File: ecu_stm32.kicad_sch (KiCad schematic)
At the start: 11 parts, among them J3 ARM Cortex Debug, U8 AZ1117-3.3

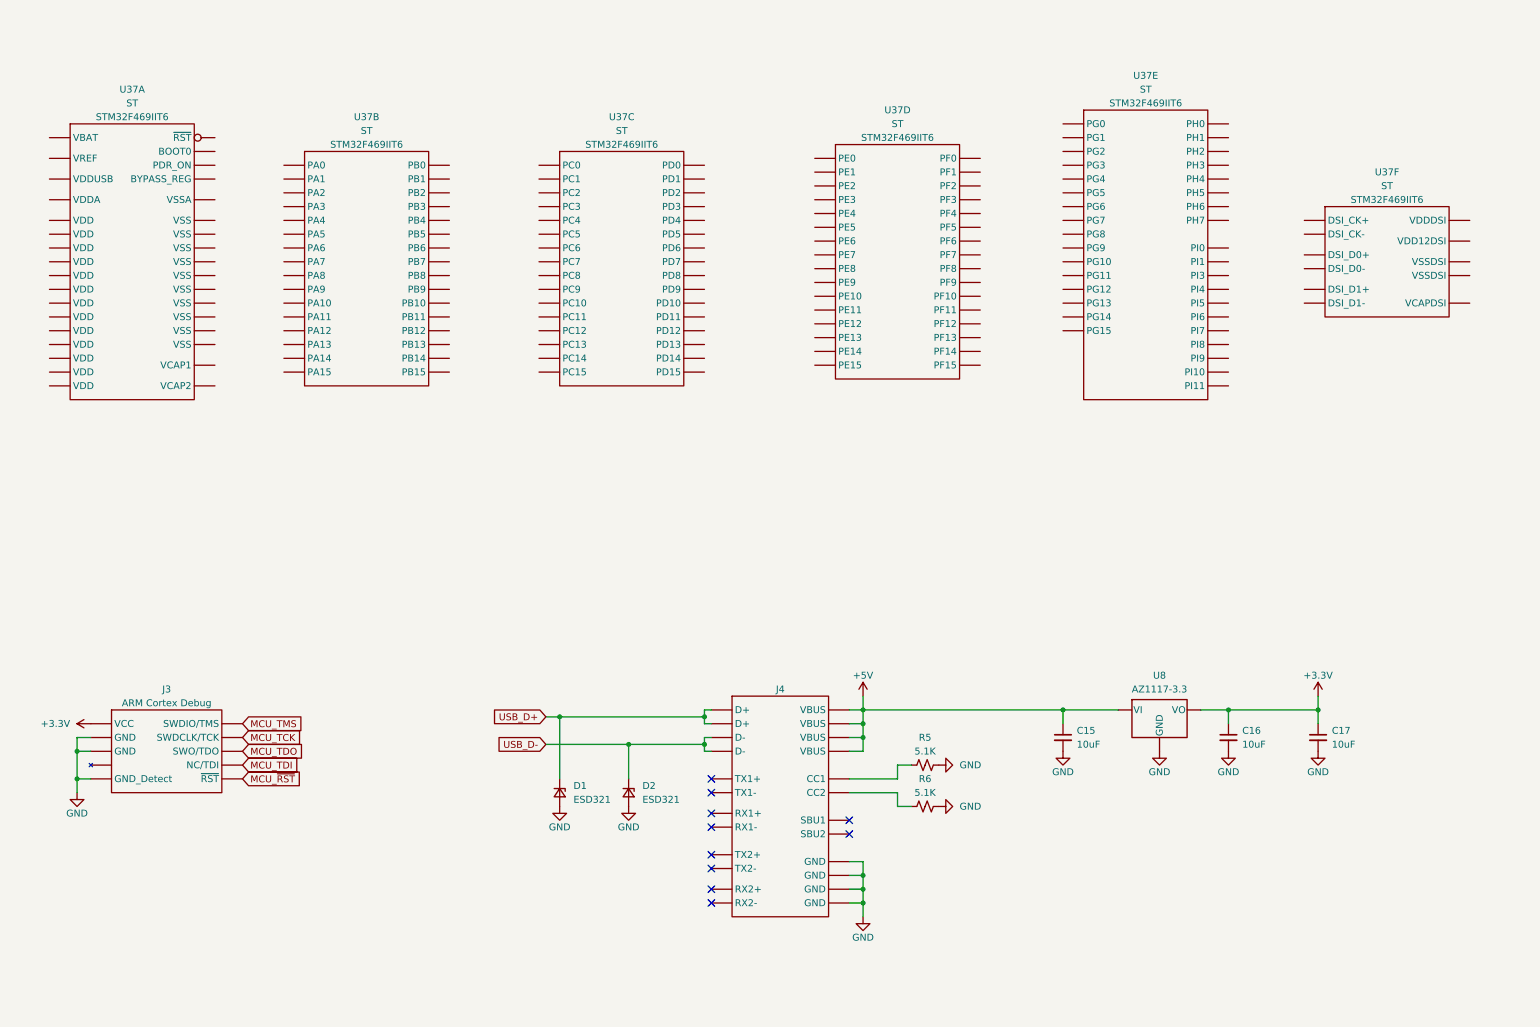
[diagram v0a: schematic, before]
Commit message: changed usb-c, re-named and added some pins
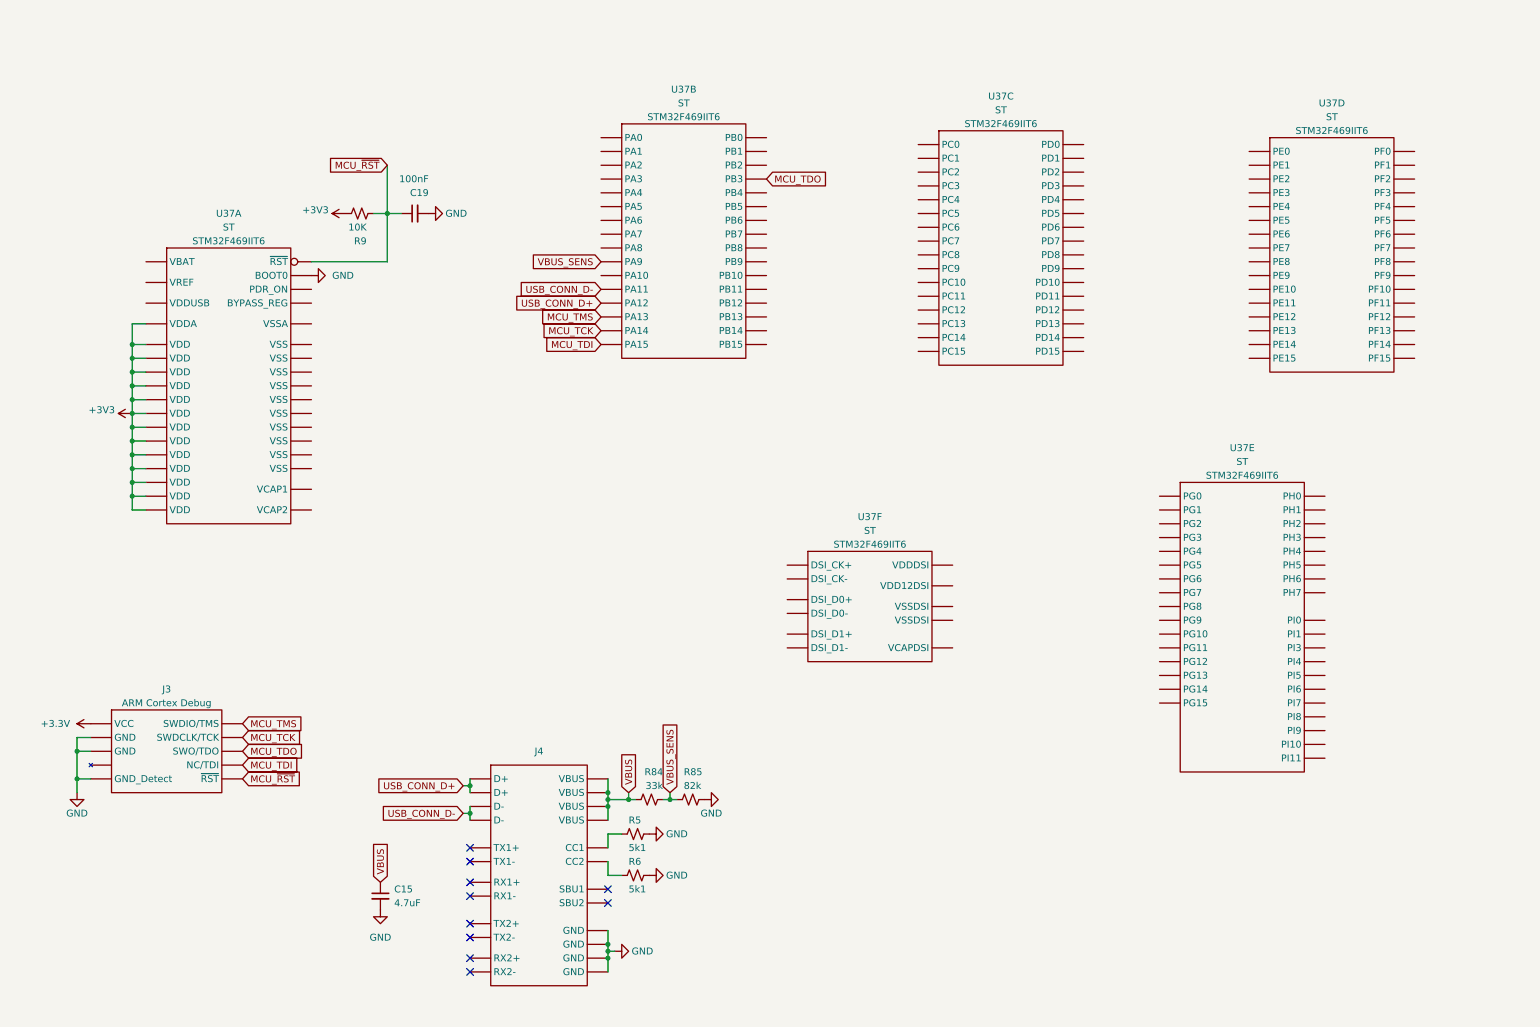
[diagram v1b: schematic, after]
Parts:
- removed C16, C17: 10uF, Capacitor_SMD:C_0603_1608Metric, symbol Device:C_Small
- removed D1, D2: ESD321, Diode_SMD:D_0402_1005Metric, symbol Device:D_Zener_Small
- removed U8: AZ1117-3.3, Package_TO_SOT_SMD:SOT-223-3_TabPin2, symbol Regulator_Linear:AZ1117-3.3
- added C19: 100nF, Capacitor_SMD:C_0603_1608Metric_Pad1.08x0.95mm_HandSolder, symbol Device:C_Small
- added R84: 33k, Resistor_SMD:R_0603_1608Metric, symbol Device:R_Small_US
- added R85: 82k, Resistor_SMD:R_0603_1608Metric, symbol Device:R_Small_US
- added R9: 10K, Resistor_SMD:R_0603_1608Metric_Pad0.98x0.95mm_HandSolder, symbol Device:R_Small_US
- C15: value 10uF -> 4.7uF; Part # Generic 0603 10uF 6.3V X7R MLCC -> Generic 0603 6.3V 4.7uF X7R MLCC
- R5, R6: value 5.1K -> 5k1; Part # Generic 0603 5.1K 1% Resistor -> Generic 0603 5.1k 1% Resistor
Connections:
- net USB_D+ is gone; now on net USB_CONN_D+: J4.A6 (D+), J4.B6 (D+)
- net USB_D- is gone; now on net USB_CONN_D-: J4.A7 (D-), J4.B7 (D-)
- net GND: now also R5.1, R6.1, U37.166 (BOOT0), C19.2, R85.1; no longer R5.2, R6.2
- net MCU_TCK: now also U37.137 (PA14)
- net MCU_TDI: now also U37.138 (PA15)
- net MCU_TDO: now also U37.161 (PB3)
- net MCU_TMS: now also U37.128 (PA13)
- net MCU_~{RST}: now also U37.31 (~{RST}), C19.1, R9.2
- net at J4.B5 (CC2): now also R6.2; no longer R6.1
- net +3V3: now reaches U37.131 (VDD)
- net +3V3: now also U37.136 (VDD), U37.149 (VDD), U37.15 (VDD), U37.159 (VDD), U37.172 (VDD), U37.23 (VDD), U37.36 (VDD), U37.39 (VDDA), U37.49 (VDD), U37.62 (VDD), U37.72 (VDD), U37.82 (VDD), U37.96 (VDD), R9.1
- net at J4.A5 (CC1): now also R5.2; no longer R5.1
- net VBUS_SENS: now reaches U37.124 (PA9)
- net VBUS_SENS: now also R84.2, R85.2
- net USB_CONN_D-: now reaches U37.126 (PA11)
- net USB_CONN_D+: now reaches U37.127 (PA12)
- net +5V renamed VBUS
- net VBUS: now also R84.1
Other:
- moved on the sheet: U37A, U37B, U37C, U37D, U37E, U37F

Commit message: added pin assignments to components on existing schematic
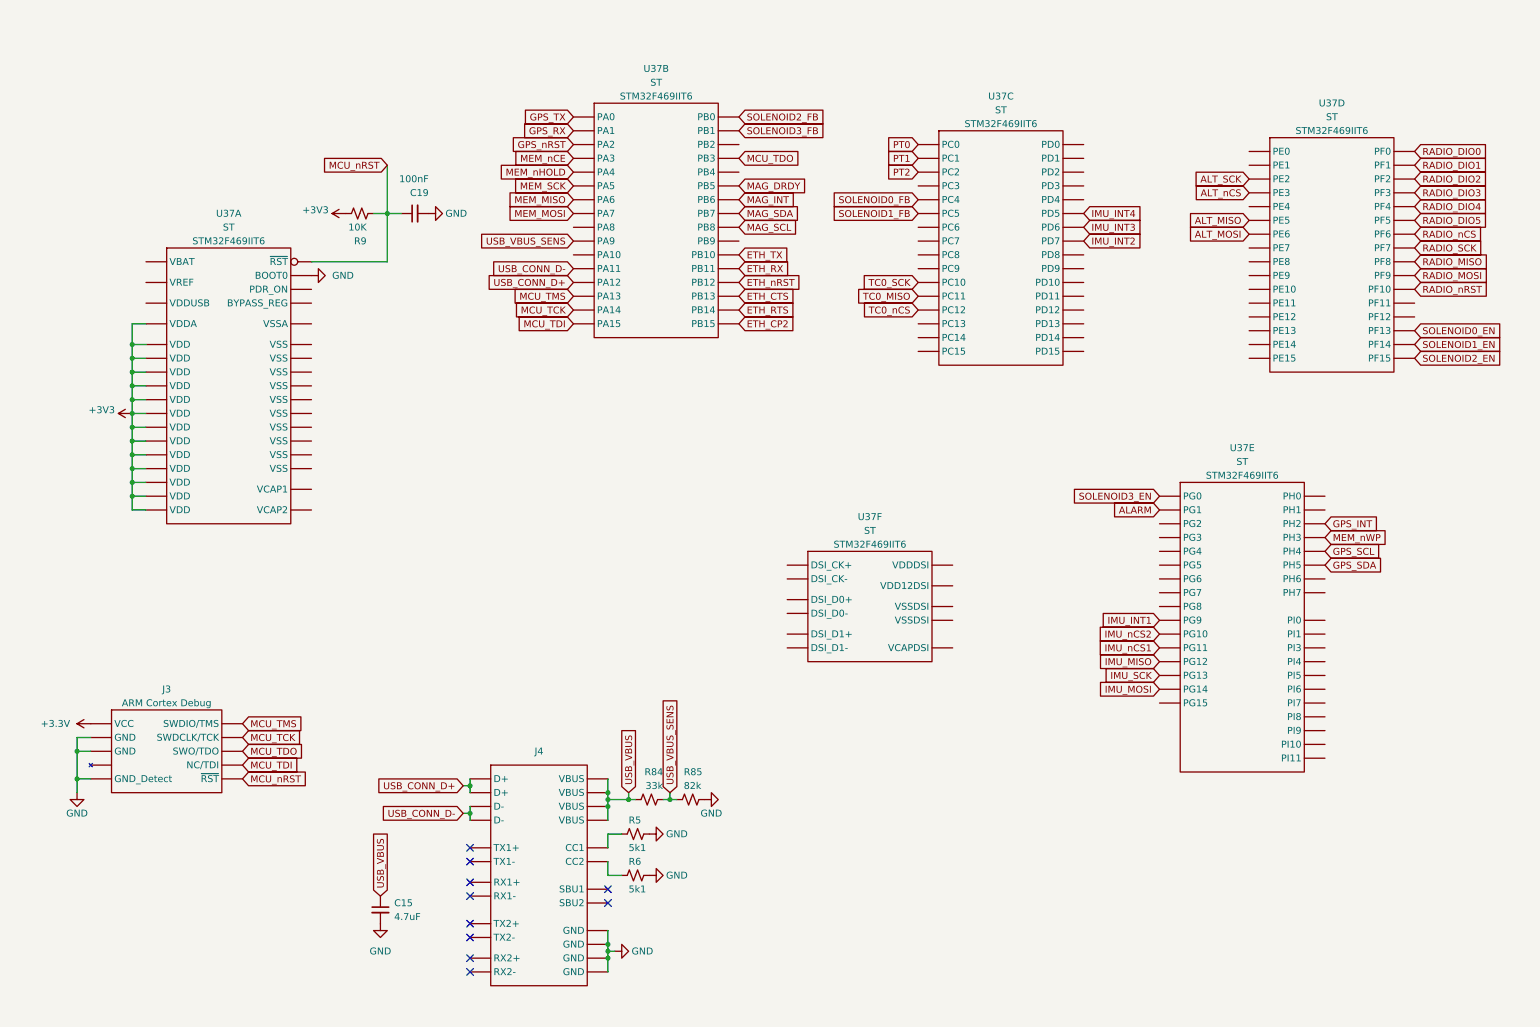
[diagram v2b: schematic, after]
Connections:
- net TC0_SCK: now reaches U37.139 (PC10)
- net TC0_MISO: now reaches U37.140 (PC11)
- net TC0_nCS: now reaches U37.141 (PC12)
- net IMU_INT4: now reaches U37.147 (PD5)
- net IMU_INT3: now reaches U37.150 (PD6)
- net IMU_INT2: now reaches U37.151 (PD7)
- net PT0: now reaches U37.32 (PC0)
- net PT1: now reaches U37.33 (PC1)
- net PT2: now reaches U37.34 (PC2)
- net SOLENOID0_FB: now reaches U37.54 (PC4)
- net SOLENOID1_FB: now reaches U37.55 (PC5)
- net IMU_INT1: now reaches U37.152 (PG9)
- net IMU_nCS2: now reaches U37.153 (PG10)
- net IMU_nCS1: now reaches U37.154 (PG11)
- net IMU_MISO: now reaches U37.155 (PG12)
- net IMU_SCK: now reaches U37.156 (PG13)
- net IMU_MOSI: now reaches U37.157 (PG14)
- net GPS_INT: now reaches U37.43 (PH2)
- net MEM_nWP: now reaches U37.44 (PH3)
- net GPS_SCL: now reaches U37.45 (PH4)
- net GPS_SDA: now reaches U37.46 (PH5)
- net SOLENOID3_EN: now reaches U37.66 (PG0)
- net ALARM: now reaches U37.67 (PG1)
- net ALT_SCK: now reaches U37.1 (PE2)
- net RADIO_DIO0: now reaches U37.16 (PF0)
- net RADIO_DIO1: now reaches U37.17 (PF1)
- net RADIO_DIO2: now reaches U37.18 (PF2)
- net RADIO_DIO3: now reaches U37.19 (PF3)
- net ALT_nCS: now reaches U37.2 (PE3)
- net RADIO_DIO4: now reaches U37.20 (PF4)
- net RADIO_DIO5: now reaches U37.21 (PF5)
- net RADIO_nCS: now reaches U37.24 (PF6)
- net RADIO_SCK: now reaches U37.25 (PF7)
- net RADIO_MISO: now reaches U37.26 (PF8)
- net RADIO_MOSI: now reaches U37.27 (PF9)
- net RADIO_nRST: now reaches U37.28 (PF10)
- net ALT_MISO: now reaches U37.4 (PE5)
- net ALT_MOSI: now reaches U37.5 (PE6)
- net SOLENOID0_EN: now reaches U37.63 (PF13)
- net SOLENOID1_EN: now reaches U37.64 (PF14)
- net SOLENOID2_EN: now reaches U37.65 (PF15)
- net MAG_DRDY: now reaches U37.163 (PB5)
- net MAG_INT: now reaches U37.164 (PB6)
- net MAG_SDA: now reaches U37.165 (PB7)
- net MAG_SCL: now reaches U37.167 (PB8)
- net GPS_TX: now reaches U37.40 (PA0)
- net GPS_RX: now reaches U37.41 (PA1)
- net GPS_nRST: now reaches U37.42 (PA2)
- net MEM_nCE: now reaches U37.47 (PA3)
- net MEM_nHOLD: now reaches U37.50 (PA4)
- net MEM_SCK: now reaches U37.51 (PA5)
- net MEM_MISO: now reaches U37.52 (PA6)
- net MEM_MOSI: now reaches U37.53 (PA7)
- net SOLENOID2_FB: now reaches U37.56 (PB0)
- net SOLENOID3_FB: now reaches U37.57 (PB1)
- net ETH_TX: now reaches U37.79 (PB10)
- net ETH_RX: now reaches U37.80 (PB11)
- net ETH_nRST: now reaches U37.85 (PB12)
- net ETH_CTS: now reaches U37.86 (PB13)
- net ETH_RTS: now reaches U37.87 (PB14)
- net ETH_CP2: now reaches U37.88 (PB15)
- net MCU_~{RST} renamed MCU_nRST
- net VBUS renamed USB_VBUS
- net VBUS_SENS renamed USB_VBUS_SENS
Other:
- moved on the sheet: C15, U37B

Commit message: Updated so only STM pins left really
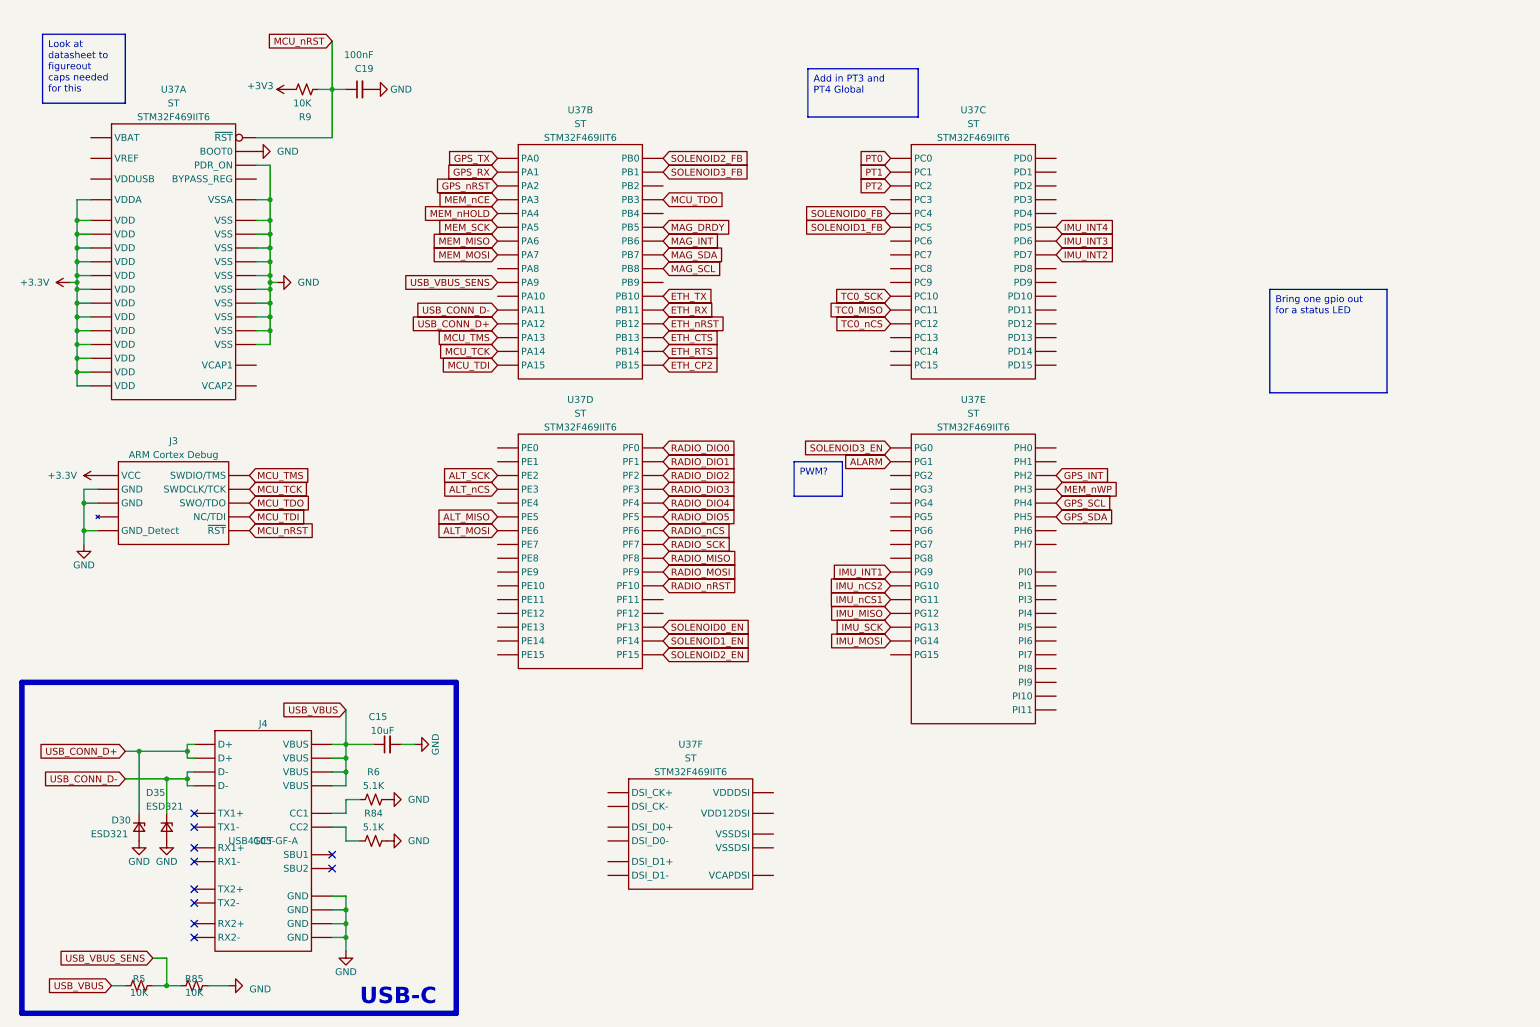
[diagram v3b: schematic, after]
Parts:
- removed J4: ~, Connector_USB:USB_C_Receptacle_GCT_USB4105-xx-A_16P_TopMnt_Horizontal, symbol UCIRP-KiCAD-Lib:USB-C
- added D30, D35: ESD321, Diode_SMD:D_0402_1005Metric, symbol Device:D_Zener_Small
- added J4: ~, Connector_USB:USB_C_Receptacle_GCT_USB4105-xx-A_16P_TopMnt_Horizontal, symbol 0INSP-KICAD-LIB:USB-C
- C15: value 4.7uF -> 10uF; Part # Generic 0603 6.3V 4.7uF X7R MLCC -> Generic 0603 10uF 6.3V X7R MLCC
- R5: value 5k1 -> 10K; footprint Resistor_SMD:R_0603_1608Metric -> Resistor_SMD:R_0603_1608Metric_Pad0.98x0.95mm_HandSolder; Part # Generic 0603 5.1k 1% Resistor -> Generic 0603 10K 1% Resistor
- R6: value 5k1 -> 5.1K; footprint Resistor_SMD:R_0603_1608Metric -> Resistor_SMD:R_0603_1608Metric_Pad0.98x0.95mm_HandSolder; Part # Generic 0603 5.1k 1% Resistor -> Generic 0603 5.1K 1% Resistor
- R84: value 33k -> 5.1K; footprint Resistor_SMD:R_0603_1608Metric -> Resistor_SMD:R_0603_1608Metric_Pad0.98x0.95mm_HandSolder; Part # Generic 0603 33k 1% Resistor -> Generic 0603 5.1K 1% Resistor
- R85: value 82k -> 10K; footprint Resistor_SMD:R_0603_1608Metric -> Resistor_SMD:R_0603_1608Metric_Pad0.98x0.95mm_HandSolder; Part # Generic 0603 82k 1% Resistor -> Generic 0603 10K 1% Resistor
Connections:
- net +3.3V: now also U37.131 (VDD), U37.136 (VDD), U37.149 (VDD), U37.15 (VDD), U37.159 (VDD), U37.172 (VDD), U37.23 (VDD), U37.36 (VDD), U37.39 (VDDA), U37.49 (VDD), U37.62 (VDD), U37.72 (VDD), U37.82 (VDD), U37.96 (VDD)
- net +3V3: no longer U37.131 (VDD), U37.136 (VDD), U37.149 (VDD), U37.15 (VDD), U37.159 (VDD), U37.172 (VDD), U37.23 (VDD), U37.36 (VDD), U37.39 (VDDA), U37.49 (VDD), U37.62 (VDD), U37.72 (VDD), U37.82 (VDD), U37.96 (VDD)
- net GND: now also R6.2, R84.2, R85.2, U37.117 (VSS), U37.130 (VSS), U37.135 (VSS), U37.14 (VSS), U37.148 (VSS), U37.158 (VSS), U37.171 (PDR_ON), U37.22 (VSS), U37.37 (VSSA), U37.61 (VSS), U37.71 (VSS), U37.95 (VSS), D30.2 (A), D35.2 (A), J4.A1 (GND), J4.A12 (GND), J4.B1 (GND), J4.B12 (GND); no longer R5.1, R6.1, R85.1
- net USB_CONN_D+: now also D30.1 (K), J4.A6 (D+), J4.B6 (D+)
- net USB_CONN_D-: now also D35.1 (K), J4.A7 (D-), J4.B7 (D-)
- net USB_VBUS: now also R5.1, J4.A4 (VBUS), J4.A9 (VBUS), J4.B4 (VBUS), J4.B9 (VBUS); no longer R84.1
- net USB_VBUS_SENS: now also R5.2, R85.1; no longer R84.2, R85.2
- new net: J4.A5 (CC1), R6.1
- new net: J4.B5 (CC2), R84.1
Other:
- note added: "USB-C"
- moved on the sheet: C19, J3, R9, U37A, U37B, U37C, U37D, U37E, U37F

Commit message: added capacitors and resolved all comments
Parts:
- added C54, C57, C78: 2.2uF, Capacitor_SMD:C_0603_1608Metric, symbol Device:C_Small
- added C58, C59, C60, C61, C62, C63, C64, C65, C66, C67, C68, C69, C70, C71, C72, C73, C74, C75, C76, C77, C79, C81, C83: 100nF, Capacitor_SMD:C_0603_1608Metric, symbol Device:C_Small
- added C80, C82: 1uF, Capacitor_SMD:C_0603_1608Metric, symbol Device:C_Small
- added C84: 4.7uF, Capacitor_SMD:C_0603_1608Metric, symbol Device:C_Small
- added R91: 10K, Resistor_SMD:R_0603_1608Metric_Pad0.98x0.95mm_HandSolder, symbol Device:R_Small_US
- added R92: 100, Resistor_SMD:R_0603_1608Metric_Pad0.98x0.95mm_HandSolder, symbol Device:R_Small_US
- renumbered C19 to C16, R9 to R86
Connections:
- net +3.3V: now also U37.118 (VDDUSB), U37.38 (VREF), U37.6 (VBAT), C58.2, C59.2, C60.2, C61.2, C62.2, C63.2, C64.2, C65.2, C66.2, C67.2, C68.2, C69.2, C70.2, C71.2, C72.2, C73.2, C74.2, C75.2, C76.2, C77.2, C79.2, C80.2, C81.2, C82.2, C83.2, C84.2
- net ALARM: now also U37.70 (PE9); no longer U37.67 (PG1)
- net GND: now also U37.103 (VSSDSI), U37.109 (VSSDSI), U37.99 (VDDDSI), C54.1, C57.1, C58.1, C59.1, C60.1, C61.1, C62.1, C63.1, C64.1, C65.1, C66.1, C67.1, C68.1, C69.1, C70.1, C71.1, C72.1, C73.1, C74.1, C75.1, C76.1, C77.1, C78.1, C79.1, C80.1, C81.1, C82.1, C83.1, C84.1, R91.2, R92.1
- net PT0: now also U37.28 (PF10); no longer U37.32 (PC0)
- net PT1: now also U37.32 (PC0); no longer U37.33 (PC1)
- net PT2: now also U37.33 (PC1); no longer U37.34 (PC2)
- net RADIO_nRST: now also U37.13 (PI11); no longer U37.28 (PF10)
- net PT4: now reaches U37.35 (PC3)
- net at U37.129 (VCAP2): now also C78.2
- net at U37.48 (BYPASS_REG): now also R91.1
- net at U37.81 (VCAP1): now also C57.2
- net at U37.100 (VCAPDSI): now also U37.106 (VDD12DSI), C54.2
- net STATUS_LED: now reaches U37.113 (PG5)
- net STATUS_LED: now also R92.2
- new net PT3: U37.34 (PC2)
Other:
- note added: "POWER SUPPLY SCHEME + SWD"
- moved on the sheet: C16, J3, R86, U37A, U37B, U37C, U37D, U37E, U37F
